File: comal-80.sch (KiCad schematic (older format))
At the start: 15 parts, among them U1 AT27C256R-150PU, U2 AT27C256R-150PU, U3 AT27C256R-150PU, U4 74LS86, U5 74LS161, U6 74LS139

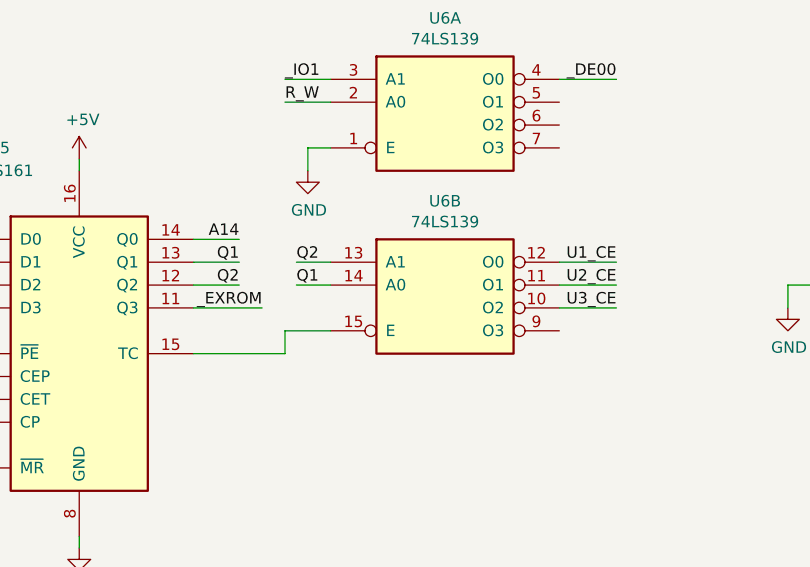
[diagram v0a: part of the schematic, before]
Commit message: Schematic Housekeeping
Adjustments made to schematic, updated PDF
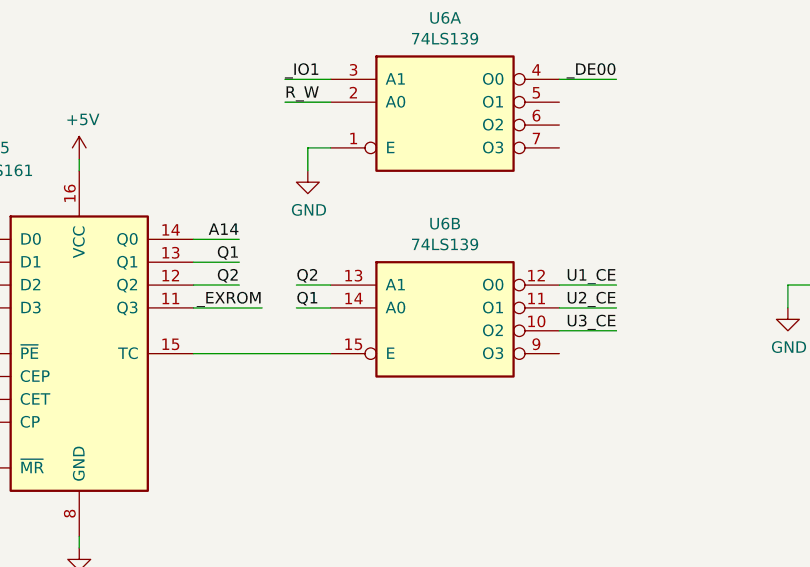
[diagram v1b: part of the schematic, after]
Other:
- moved on the sheet: U6B
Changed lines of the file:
@@
 L 74xx:74LS139 U6
 U 2 1 5FD665B3
-P 7100 4250
-F 0 "U6" H 7100 4617 50  0000 C CNN
-F 1 "74LS139" H 7100 4526 50  0000 C CNN
-F 2 "Package_DIP:DIP-16_W7.62mm_Socket" H 7100 4250 50  0001 C CNN
-F 3 "http://www.ti.com/lit/ds/symlink/sn74ls139a.pdf" H 7100 4250 50  0001 C CNN
-	2    7100 4250
+P 7100 4350
+F 0 "U6" H 7100 4717 50  0000 C CNN
+F 1 "74LS139" H 7100 4626 50  0000 C CNN
+F 2 "Package_DIP:DIP-16_W7.62mm_Socket" H 7100 4350 50  0001 C CNN
+F 3 "http://www.ti.com/lit/ds/symlink/sn74ls139a.pdf" H 7100 4350 50  0001 C CNN
+	2    7100 4350
 	1    0    0    -1
 $EndComp
@@
 _DE00
 Wire Wire Line
-	6000 4550 6400 4550
-Wire Wire Line
-	6400 4550 6400 4450
-Wire Wire Line
-	6400 4450 6600 4450
-Wire Wire Line
 	6000 4350 6300 4350
 Text Label 6300 4350 2    50   ~ 0
@@
 $EndComp
 Wire Wire Line
-	7600 4150 7850 4150
-Text Label 7850 4150 2    50   ~ 0
+	7600 4250 7850 4250
+Text Label 7850 4250 2    50   ~ 0
 U1_CE
 Wire Wire Line
-	7600 4250 7850 4250
-Wire Wire Line
 	7600 4350 7850 4350
-Text Label 7850 4250 2    50   ~ 0
+Wire Wire Line
+	7600 4450 7850 4450
+Text Label 7850 4350 2    50   ~ 0
 U2_CE
-Text Label 7850 4350 2    50   ~ 0
+Text Label 7850 4450 2    50   ~ 0
 U3_CE
 Wire Wire Line
@@
 $EndComp
 Wire Wire Line
+	6450 4350 6600 4350
+Wire Wire Line
+	6000 4150 6200 4150
+Wire Wire Line
 	6450 4250 6600 4250
 Wire Wire Line
-	6000 4150 6200 4150
-Wire Wire Line
-	6450 4150 6600 4150
-Wire Wire Line
 	6000 4250 6200 4250
-Text Label 6450 4150 0    50   ~ 0
+Text Label 6450 4250 0    50   ~ 0
 Q2
-Text Label 6450 4250 0    50   ~ 0
+Text Label 6450 4350 0    50   ~ 0
 Q1
 Text Label 6200 4150 2    50   ~ 0
@@
 	1    0    0    -1
 $EndComp
+Wire Wire Line
+	6000 4550 6600 4550
 $EndSCHEMATC
